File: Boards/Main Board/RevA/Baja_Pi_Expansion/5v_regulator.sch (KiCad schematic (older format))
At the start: 7 parts

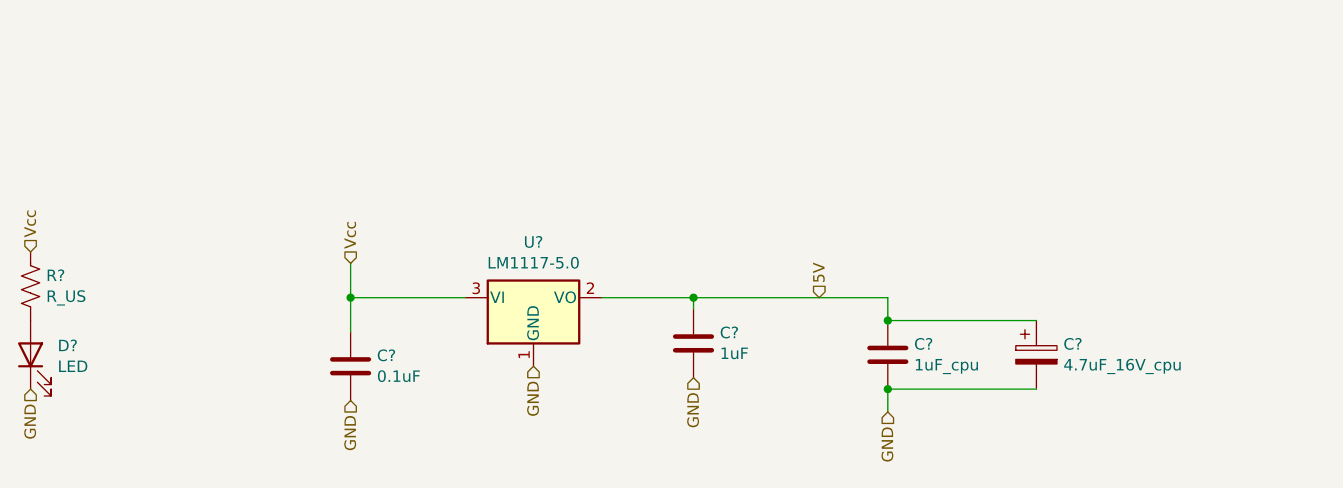
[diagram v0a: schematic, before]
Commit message: Added a Majority of Main Board Footprints
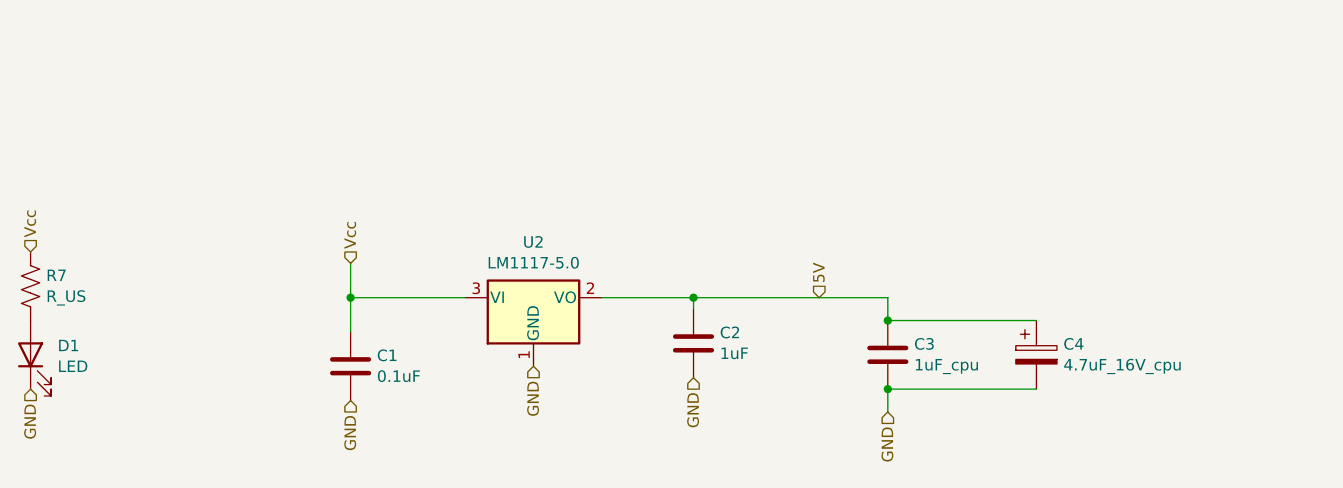
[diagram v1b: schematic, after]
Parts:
- C1, C2, C3: renamed from C?; footprint (none) -> Capacitor_SMD:C_0603_1608Metric
- R7: renamed from R?; footprint (none) -> Resistor_SMD:R_0603_1608Metric
- gave numbers to parts that had none: 3
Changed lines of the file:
@@
 P 2550 2800
 AR Path="/61653277" Ref="R?"  Part="1"
-AR Path="/6164E083/61653277" Ref="R?"  Part="1"
-F 0 "R?" H 2618 2846 50  0000 L CNN
+AR Path="/6164E083/61653277" Ref="R7"  Part="1"
+F 0 "R7" H 2618 2846 50  0000 L CNN
 F 1 "R_US" H 2618 2755 50  0000 L CNN
-F 2 "" V 2590 2790 50  0001 C CNN
+F 2 "Resistor_SMD:R_0603_1608Metric" V 2590 2790 50  0001 C CNN
 F 3 "~" H 2550 2800 50  0001 C CNN
 	1    2550 2800
@@
 P 2550 3100
 AR Path="/6165327D" Ref="D?"  Part="1"
-AR Path="/6164E083/6165327D" Ref="D?"  Part="1"
-F 0 "D?" V 2589 2982 50  0000 R CNN
+AR Path="/6164E083/6165327D" Ref="D1"  Part="1"
+F 0 "D1" V 2589 2982 50  0000 R CNN
 F 1 "LED" V 2498 2982 50  0000 R CNN
 F 2 "" H 2550 3100 50  0001 C CNN
@@
 GND
 $Comp
-L Regulator_Linear:LM1117-5.0 U?
+L Regulator_Linear:LM1117-5.0 U2
 U 1 1 616546A9
 P 4750 2850
-F 0 "U?" H 4750 3092 50  0000 C CNN
+F 0 "U2" H 4750 3092 50  0000 C CNN
 F 1 "LM1117-5.0" H 4750 3001 50  0000 C CNN
 F 2 "" H 4750 2850 50  0001 C CNN
@@
 $EndComp
 $Comp
-L Device:C C?
+L Device:C C1
 U 1 1 61655F33
 P 3950 3150
-F 0 "C?" H 4065 3196 50  0000 L CNN
+F 0 "C1" H 4065 3196 50  0000 L CNN
 F 1 "0.1uF" H 4065 3105 50  0000 L CNN
-F 2 "" H 3988 3000 50  0001 C CNN
+F 2 "Capacitor_SMD:C_0603_1608Metric" H 3988 3000 50  0001 C CNN
 F 3 "~" H 3950 3150 50  0001 C CNN
 	1    3950 3150
@@
 $EndComp
 $Comp
-L Device:C C?
+L Device:C C2
 U 1 1 61656877
 P 5450 3050
-F 0 "C?" H 5565 3096 50  0000 L CNN
+F 0 "C2" H 5565 3096 50  0000 L CNN
 F 1 "1uF" H 5565 3005 50  0000 L CNN
-F 2 "" H 5488 2900 50  0001 C CNN
+F 2 "Capacitor_SMD:C_0603_1608Metric" H 5488 2900 50  0001 C CNN
 F 3 "~" H 5450 3050 50  0001 C CNN
 	1    5450 3050
@@
 $EndComp
 $Comp
-L Device:C C?
+L Device:C C3
 U 1 1 6165740F
 P 6300 3100
-F 0 "C?" H 6415 3146 50  0000 L CNN
+F 0 "C3" H 6415 3146 50  0000 L CNN
 F 1 "1uF_cpu" H 6415 3055 50  0000 L CNN
-F 2 "" H 6338 2950 50  0001 C CNN
+F 2 "Capacitor_SMD:C_0603_1608Metric" H 6338 2950 50  0001 C CNN
 F 3 "~" H 6300 3100 50  0001 C CNN
 	1    6300 3100
@@
 $EndComp
 $Comp
-L Device:CP C?
+L Device:CP C4
 U 1 1 6165888C
 P 6950 3100
-F 0 "C?" H 7068 3146 50  0000 L CNN
+F 0 "C4" H 7068 3146 50  0000 L CNN
 F 1 "4.7uF_16V_cpu" H 7068 3055 50  0000 L CNN
 F 2 "" H 6988 2950 50  0001 C CNN

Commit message: Added \#Parts
(For 5V Regulator)
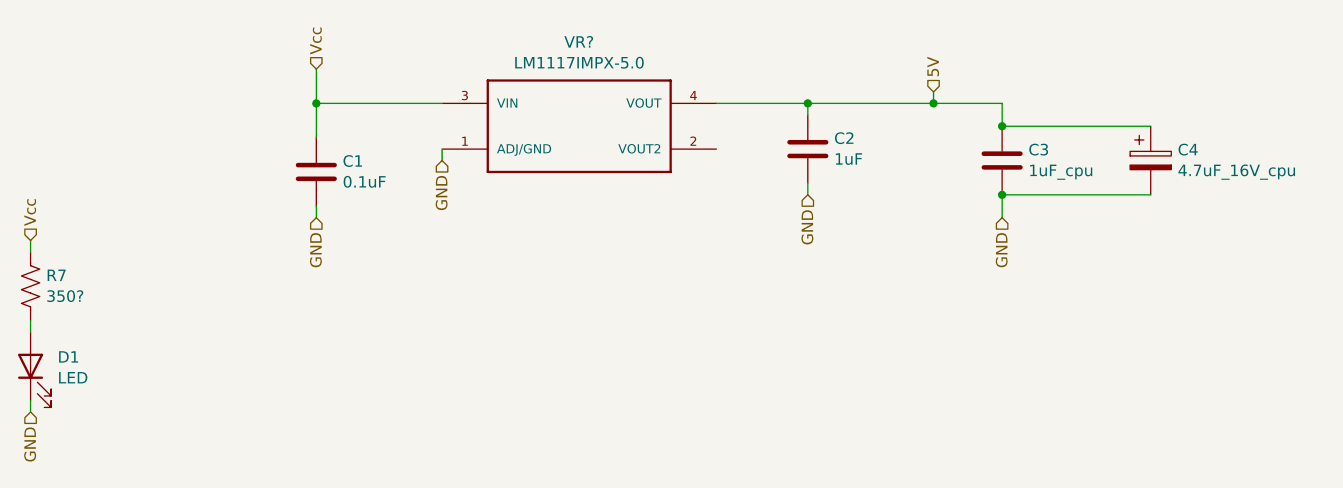
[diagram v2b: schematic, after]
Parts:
- removed U2: LM1117-5.0, symbol Regulator_Linear:LM1117-5.0
- added VR?: LM1117IMPX-5.0, SOT230P700X180-4N, symbol LM1117IMPX-5.0:LM1117IMPX-5.0
- R7: value R_US -> 350?
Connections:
- net 5V: now also VR?.4 (VOUT)
- net GND: now also VR?.1 (ADJ/GND)
- net Vcc: now also VR?.3 (VIN)
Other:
- moved on the sheet: C1, C2, C3, C4, D1
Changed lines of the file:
@@
 AR Path="/6164E083/61653277" Ref="R7"  Part="1"
 F 0 "R7" H 2618 2846 50  0000 L CNN
-F 1 "R_US" H 2618 2755 50  0000 L CNN
+F 1 "350?" H 2618 2755 50  0000 L CNN
 F 2 "Resistor_SMD:R_0603_1608Metric" V 2590 2790 50  0001 C CNN
 F 3 "~" H 2550 2800 50  0001 C CNN
@@
 L Device:LED D?
 U 1 1 6165327D
-P 2550 3100
+P 2550 3150
 AR Path="/6165327D" Ref="D?"  Part="1"
 AR Path="/6164E083/6165327D" Ref="D1"  Part="1"
-F 0 "D1" V 2589 2982 50  0000 R CNN
-F 1 "LED" V 2498 2982 50  0000 R CNN
-F 2 "" H 2550 3100 50  0001 C CNN
-F 3 "~" H 2550 3100 50  0001 C CNN
-	1    2550 3100
+F 0 "D1" V 2589 3032 50  0000 R CNN
+F 1 "LED" V 2498 3032 50  0000 R CNN
+F 2 "" H 2550 3150 50  0001 C CNN
+F 3 "~" H 2550 3150 50  0001 C CNN
+	1    2550 3150
 	0    -1   -1   0
 $EndComp
-Text HLabel 2550 2650 1    50   Input ~ 0
+Text HLabel 2550 2600 1    50   Input ~ 0
 Vcc
-Text HLabel 2550 3250 3    50   Input ~ 0
+Text HLabel 2550 3350 3    50   Input ~ 0
 GND
-$Comp
-L Regulator_Linear:LM1117-5.0 U2
-U 1 1 616546A9
-P 4750 2850
-F 0 "U2" H 4750 3092 50  0000 C CNN
-F 1 "LM1117-5.0" H 4750 3001 50  0000 C CNN
-F 2 "" H 4750 2850 50  0001 C CNN
-F 3 "http://www.ti.com/lit/ds/symlink/lm1117.pdf" H 4750 2850 50  0001 C CNN
-	1    4750 2850
-	1    0    0    -1
-$EndComp
 $Comp
 L Device:C C1
 U 1 1 61655F33
-P 3950 3150
-F 0 "C1" H 4065 3196 50  0000 L CNN
-F 1 "0.1uF" H 4065 3105 50  0000 L CNN
-F 2 "Capacitor_SMD:C_0603_1608Metric" H 3988 3000 50  0001 C CNN
-F 3 "~" H 3950 3150 50  0001 C CNN
-	1    3950 3150
+P 3800 2300
+F 0 "C1" H 3915 2346 50  0000 L CNN
+F 1 "0.1uF" H 3915 2255 50  0000 L CNN
+F 2 "Capacitor_SMD:C_0603_1608Metric" H 3838 2150 50  0001 C CNN
+F 3 "~" H 3800 2300 50  0001 C CNN
+	1    3800 2300
 	1    0    0    -1
 $EndComp
@@
 L Device:C C2
 U 1 1 61656877
-P 5450 3050
-F 0 "C2" H 5565 3096 50  0000 L CNN
-F 1 "1uF" H 5565 3005 50  0000 L CNN
-F 2 "Capacitor_SMD:C_0603_1608Metric" H 5488 2900 50  0001 C CNN
-F 3 "~" H 5450 3050 50  0001 C CNN
-	1    5450 3050
+P 5950 2200
+F 0 "C2" H 6065 2246 50  0000 L CNN
+F 1 "1uF" H 6065 2155 50  0000 L CNN
+F 2 "Capacitor_SMD:C_0603_1608Metric" H 5988 2050 50  0001 C CNN
+F 3 "~" H 5950 2200 50  0001 C CNN
+	1    5950 2200
 	1    0    0    -1
 $EndComp
@@
 L Device:C C3
 U 1 1 6165740F
-P 6300 3100
-F 0 "C3" H 6415 3146 50  0000 L CNN
-F 1 "1uF_cpu" H 6415 3055 50  0000 L CNN
-F 2 "Capacitor_SMD:C_0603_1608Metric" H 6338 2950 50  0001 C CNN
-F 3 "~" H 6300 3100 50  0001 C CNN
-	1    6300 3100
+P 6800 2250
+F 0 "C3" H 6915 2296 50  0000 L CNN
+F 1 "1uF_cpu" H 6915 2205 50  0000 L CNN
+F 2 "Capacitor_SMD:C_0603_1608Metric" H 6838 2100 50  0001 C CNN
+F 3 "~" H 6800 2250 50  0001 C CNN
+	1    6800 2250
 	1    0    0    -1
 $EndComp
@@
 L Device:CP C4
 U 1 1 6165888C
-P 6950 3100
-F 0 "C4" H 7068 3146 50  0000 L CNN
-F 1 "4.7uF_16V_cpu" H 7068 3055 50  0000 L CNN
-F 2 "" H 6988 2950 50  0001 C CNN
-F 3 "~" H 6950 3100 50  0001 C CNN
-	1    6950 3100
+P 7450 2250
+F 0 "C4" H 7568 2296 50  0000 L CNN
+F 1 "4.7uF_16V_cpu" H 7568 2205 50  0000 L CNN
+F 2 "" H 7488 2100 50  0001 C CNN
+F 3 "~" H 7450 2250 50  0001 C CNN
+	1    7450 2250
 	1    0    0    -1
 $EndComp
 Wire Wire Line
-	5450 2900 5450 2850
+	5950 2050 5950 2000
 Wire Wire Line
-	5450 2850 5050 2850
-Text HLabel 5450 3200 3    50   Input ~ 0
+	5950 2000 5550 2000
+Text HLabel 5950 2400 3    50   Input ~ 0
 GND
-Text HLabel 3950 2700 1    50   Input ~ 0
+Text HLabel 3800 1850 1    50   Input ~ 0
 Vcc
-Text HLabel 3950 3300 3    50   Input ~ 0
+Text HLabel 3800 2500 3    50   Input ~ 0
 GND
 Wire Wire Line
-	4450 2850 3950 2850
+	3800 2000 3800 1850
 Wire Wire Line
-	3950 2850 3950 2700
-Wire Wire Line
-	3950 3000 3950 2850
-Connection ~ 3950 2850
-Text HLabel 6300 3350 3    50   Input ~ 0
+	3800 2150 3800 2000
+Connection ~ 3800 2000
+Text HLabel 6800 2500 3    50   Input ~ 0
 GND
 Wire Wire Line
-	6300 3350 6300 3250
+	6800 2500 6800 2400
 Wire Wire Line
-	5450 2850 6300 2850
+	5950 2000 6500 2000
 Wire Wire Line
-	6300 2850 6300 2950
-Connection ~ 5450 2850
+	6800 2000 6800 2100
+Connection ~ 5950 2000
 Wire Wire Line
-	6300 2950 6950 2950
-Connection ~ 6300 2950
+	6800 2100 7450 2100
+Connection ~ 6800 2100
 Wire Wire Line
-	6300 3250 6950 3250
-Connection ~ 6300 3250
-Text HLabel 4750 3150 3    50   Input ~ 0
+	6800 2400 7450 2400
+Connection ~ 6800 2400
+Text HLabel 4350 2250 3    50   Input ~ 0
 GND
-Text HLabel 6000 2850 1    50   Input ~ 0
+Text HLabel 6500 1950 1    50   Input ~ 0
 5V
+Wire Wire Line
+	3800 2500 3800 2450
+Wire Wire Line
+	4350 2250 4350 2200
+Wire Wire Line
+	5950 2400 5950 2350
+Wire Wire Line
+	2550 3000 2550 2950
+Wire Wire Line
+	2550 3350 2550 3300
+Wire Wire Line
+	2550 2600 2550 2650
+Wire Wire Line
+	6500 1950 6500 2000
+Connection ~ 6500 2000
+Wire Wire Line
+	6500 2000 6800 2000
+Wire Wire Line
+	3800 2000 4350 2000
+$Comp
+L LM1117IMPX-5.0:LM1117IMPX-5.0 VR?
+U 1 1 6168283C
+P 4950 2100
+F 0 "VR?" H 4950 2467 50  0000 C CNN
+F 1 "LM1117IMPX-5.0" H 4950 2376 50  0000 C CNN
+F 2 "SOT230P700X180-4N" H 4950 2100 50  0001 L BNN
+F 3 "1.80 mm" H 4950 2100 50  0001 L BNN
+F 4 "O" H 4950 2100 50  0001 L BNN "Field4"
+F 5 "IPC 7351B" H 4950 2100 50  0001 L BNN "Field5"
+F 6 "Rochester Electronics/Texas Instruments" H 4950 2100 50  0001 L BNN "Field6"
+	1    4950 2100
+	1    0    0    -1
+$EndComp
 $EndSCHEMATC

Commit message: Fixed LM1117 Symbol
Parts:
- D1: footprint (none) -> LED_SMD:LED_1812_4532Metric
- VR1: renamed from VR?; footprint SOT230P700X180-4N -> (none)
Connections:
- net 5V: now also VR1.2 (VOUT2)
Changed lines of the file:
@@
 F 0 "D1" V 2589 3032 50  0000 R CNN
 F 1 "LED" V 2498 3032 50  0000 R CNN
-F 2 "" H 2550 3150 50  0001 C CNN
+F 2 "LED_SMD:LED_1812_4532Metric" H 2550 3150 50  0001 C CNN
 F 3 "~" H 2550 3150 50  0001 C CNN
 	1    2550 3150
@@
 	3800 2000 4350 2000
 $Comp
-L LM1117IMPX-5.0:LM1117IMPX-5.0 VR?
+L LM1117IMPX-5.0:LM1117IMPX-5.0 VR1
 U 1 1 6168283C
 P 4950 2100
-F 0 "VR?" H 4950 2467 50  0000 C CNN
+F 0 "VR1" H 4950 2467 50  0000 C CNN
 F 1 "LM1117IMPX-5.0" H 4950 2376 50  0000 C CNN
-F 2 "SOT230P700X180-4N" H 4950 2100 50  0001 L BNN
+F 2 "" H 4950 2100 50  0001 L BNN
 F 3 "1.80 mm" H 4950 2100 50  0001 L BNN
 F 4 "O" H 4950 2100 50  0001 L BNN "Field4"
@@
 	1    0    0    -1
 $EndComp
+Wire Wire Line
+	5550 2200 5550 2000
+Connection ~ 5550 2000
 $EndSCHEMATC

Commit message: Created Main Board netlist
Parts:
- C4: footprint (none) -> Capacitor_Tantalum_SMD:CP_EIA-3216-18_Kemet-A
- VR1: footprint (none) -> LM1117IMPX-5:SOT230P700X180-4N
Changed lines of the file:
@@
 F 0 "C4" H 7568 2296 50  0000 L CNN
 F 1 "4.7uF_16V_cpu" H 7568 2205 50  0000 L CNN
-F 2 "" H 7488 2100 50  0001 C CNN
+F 2 "Capacitor_Tantalum_SMD:CP_EIA-3216-18_Kemet-A" H 7488 2100 50  0001 C CNN
 F 3 "~" H 7450 2250 50  0001 C CNN
 	1    7450 2250
@@
 F 0 "VR1" H 4950 2467 50  0000 C CNN
 F 1 "LM1117IMPX-5.0" H 4950 2376 50  0000 C CNN
-F 2 "" H 4950 2100 50  0001 L BNN
+F 2 "LM1117IMPX-5:SOT230P700X180-4N" H 4950 2100 50  0001 L BNN
 F 3 "1.80 mm" H 4950 2100 50  0001 L BNN
 F 4 "O" H 4950 2100 50  0001 L BNN "Field4"
